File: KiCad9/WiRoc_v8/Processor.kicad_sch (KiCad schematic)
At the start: 21 parts

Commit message: etc
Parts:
- C66, C69, C73, C76, C77, C81, C82, C83: LCSC Part # (none) -> C52923; Manufacturer (none) -> Samsung Electro-Mechanics; ManufacturerPartNumber (none) -> CL05A105KA5NQNC
- C70, C72, C75, C79: LCSC Part # (none) -> C15525; Manufacturer (none) -> Samsung Electro-Mechanics; ManufacturerPartNumber (none) -> CL05A106MQ5NUNC
- U11: value ~ -> AllwinnerH3

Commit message: add bom
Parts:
- C66, C69, C70, C72, C73, C75, C76, C77, C79, C81, C82, C83: IncludeInBOM (none) -> TRUE; JLCBasicExtended (none) -> Basic; Package (none) -> 0402
- C67, C68, C71, C74, C78, C84, C85: IncludeInBOM (none) -> TRUE; JLCBasicExtended (none) -> Basic; LCSC Part # (none) -> C1525; Manufacturer (none) -> Samsung Electro-Mechanics; ManufacturerPartNumber (none) -> CL05B104KO5NNNC; Package (none) -> 0402
- R19: IncludeInBOM (none) -> TRUE; JLCBasicExtended (none) -> Basic; LCSC Part # (none) -> C17168; Manufacturer (none) -> Uniroyal Elec; ManufacturerPartNumber (none) -> 0402WGF0000TCE; Package (none) -> 0402
- U11: IncludeInBOM (none) -> TRUE; JLCBasicExtended (none) -> Extended; LCSC Part # (none) -> C94644; Manufacturer (none) -> Allwinner; ManufacturerPartNumber (none) -> H3; Package (none) -> FBGA-347(14x14)

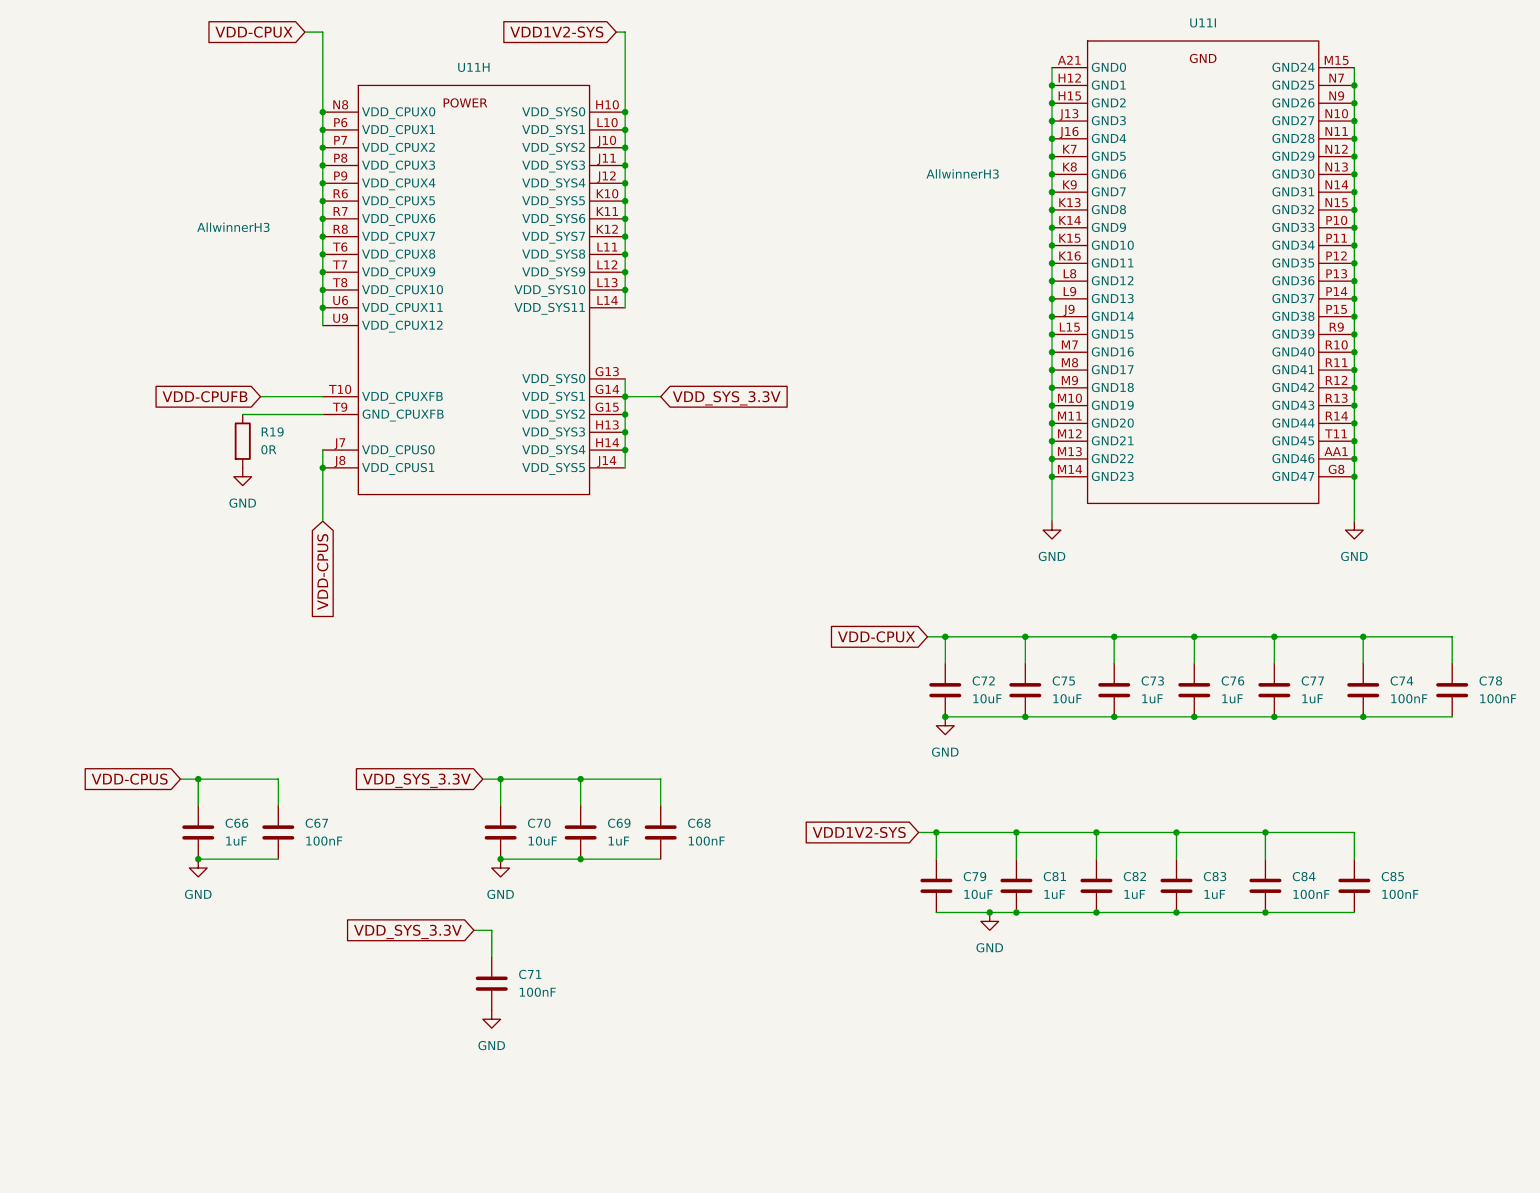
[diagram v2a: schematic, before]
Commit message: add esp32hosted-c5 board
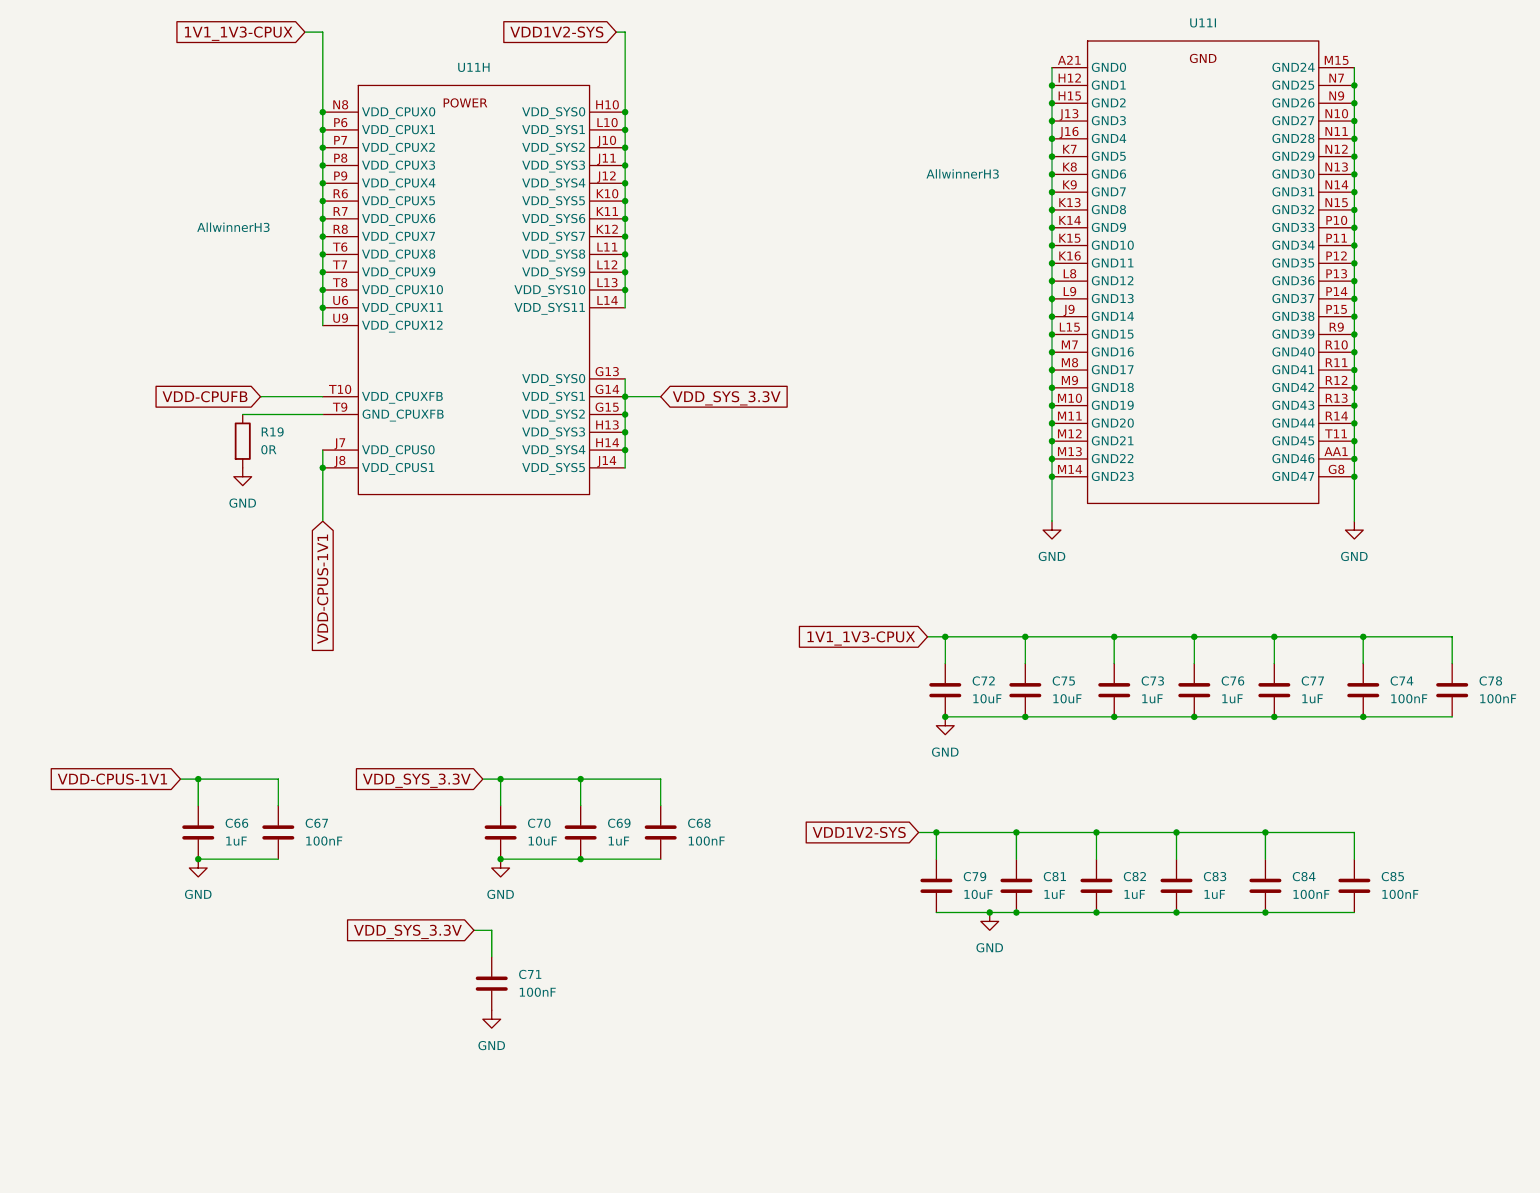
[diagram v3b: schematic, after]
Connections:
- net VDD-CPUS renamed VDD-CPUS-1V1
- net VDD-CPUX renamed 1V1_1V3-CPUX
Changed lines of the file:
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@@
 		)
 	)
-	(global_label "VDD-CPUX"
+	(global_label "1V1_1V3-CPUX"
 		(shape input)
 		(at 138.43 113.03 180)
@@
 		)
 		(property "Intersheetrefs" "${INTERSHEET_REFS}"
-			(at 123.296 113.03 0)
+			(at 118.071 113.03 0)
 			(effects
 				(font
@@
 		)
 	)
-	(global_label "VDD-CPUX"
+	(global_label "1V1_1V3-CPUX"
 		(shape input)
 		(at 49.53 26.67 180)
@@
 		)
 		(property "Intersheetrefs" "${INTERSHEET_REFS}"
-			(at 34.396 26.67 0)
+			(at 29.171 26.67 0)
 			(effects
 				(font
@@
 		)
 	)
-	(global_label "VDD-CPUS"
+	(global_label "VDD-CPUS-1V1"
 		(shape input)
 		(at 31.75 133.35 180)
@@
 		)
 		(property "Intersheetrefs" "${INTERSHEET_REFS}"
-			(at 16.616 133.35 0)
+			(at 10.52 133.35 0)
 			(effects
 				(font
@@
 		)
 	)
-	(global_label "VDD-CPUS"
+	(global_label "VDD-CPUS-1V1"
 		(shape input)
 		(at 52.07 96.52 270)
@@
 		)
 		(property "Intersheetrefs" "${INTERSHEET_REFS}"
-			(at 52.07 111.654 90)
+			(at 52.07 117.75 90)
 			(effects
 				(font

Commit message: change to 10uF in pdn, vdd-dram area to south caps, remove varistor, etc
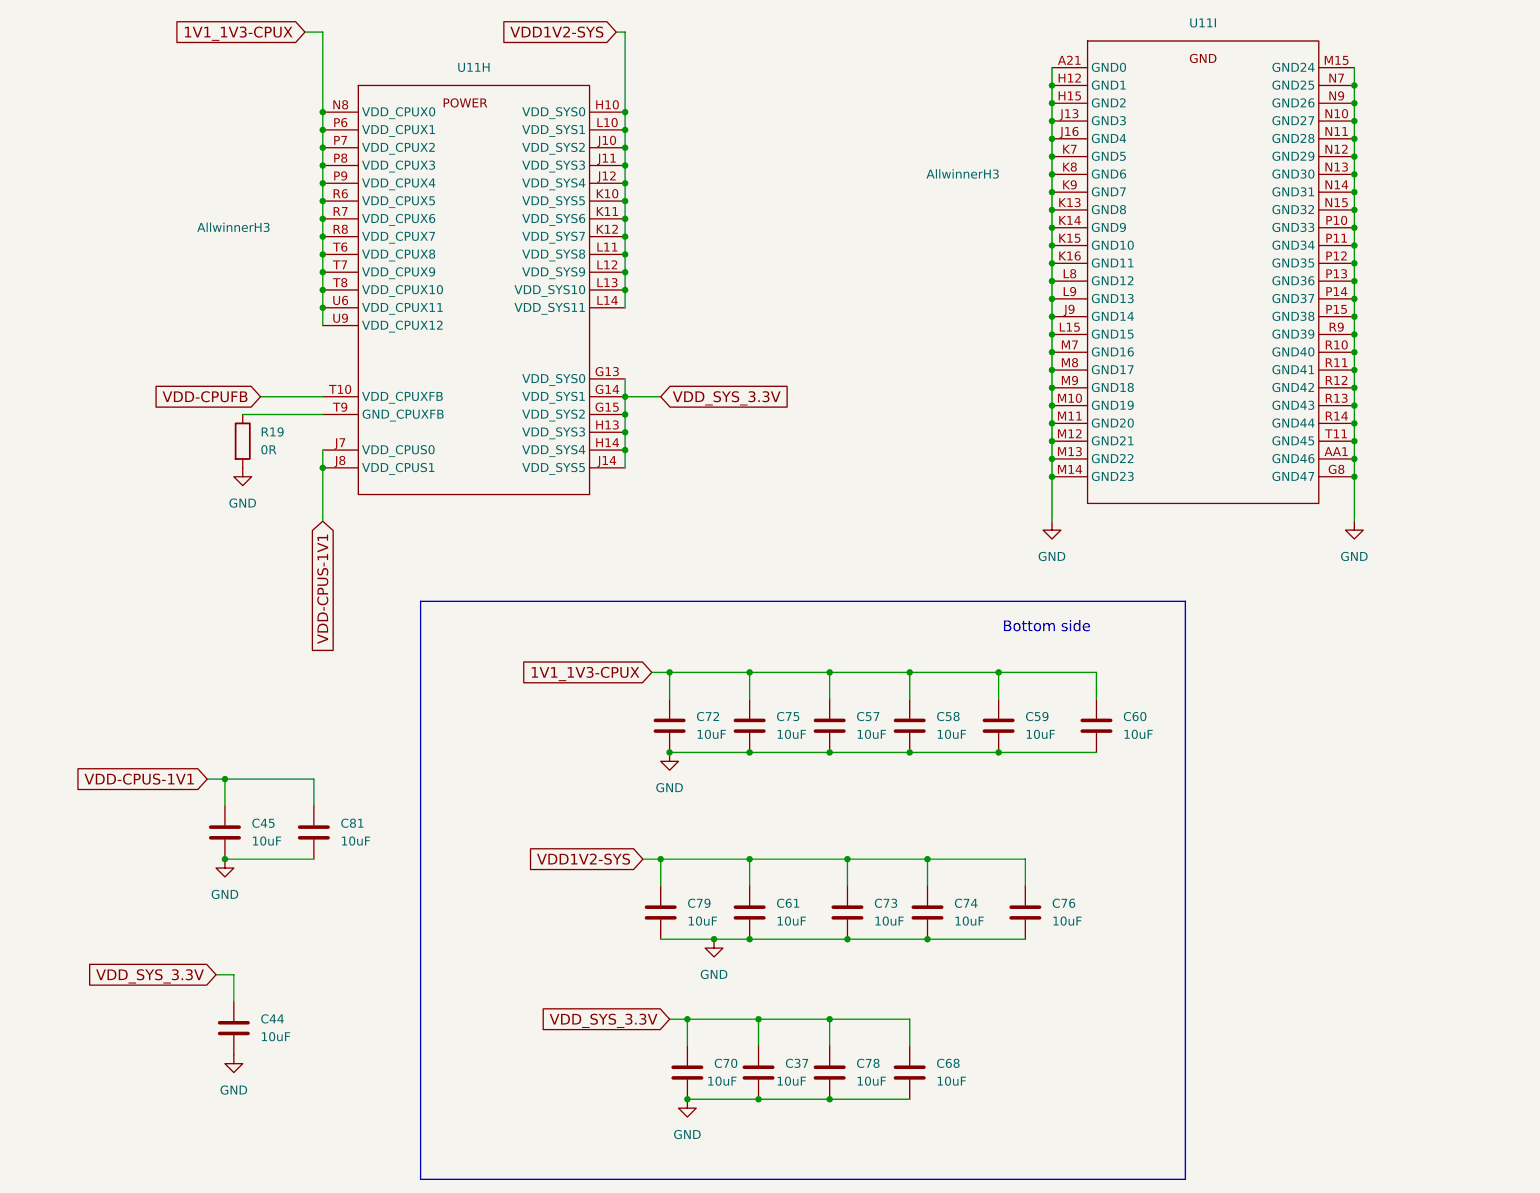
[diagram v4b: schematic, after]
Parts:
- removed C66, C69, C77, C82, C83: 1uF, Capacitor_SMD:C_0402_1005Metric, symbol Device:C
- removed C67, C71, C84, C85: 100nF, Capacitor_SMD:C_0402_1005Metric, symbol Device:C
- added C37, C44, C45, C57, C58, C59, C60, C61: 10uF, Capacitor_SMD:C_0402_1005Metric, symbol Device:C
- C68, C74, C78: value 100nF -> 10uF; LCSC Part # C1525 -> C15525; ManufacturerPartNumber CL05B104KO5NNNC -> CL05A106MQ5NUNC
- C73, C76, C81: value 1uF -> 10uF; LCSC Part # C52923 -> C15525; ManufacturerPartNumber CL05A105KA5NQNC -> CL05A106MQ5NUNC
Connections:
- net 1V1_1V3-CPUX: now also C57.1, C58.1, C59.1, C60.1; no longer C73.1, C74.1, C76.1, C78.1
- net GND: now also C37.2, C44.2, C45.2, C57.2, C58.2, C59.2, C60.2, C61.2
- net VDD-CPUS-1V1: now also C81.1, C45.1
- net VDD1V2-SYS: now also C73.1, C74.1, C76.1, C61.1; no longer C81.1
- net VDD_SYS_3.3V: now also C78.1, C37.1, C44.1
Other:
- note added: "Bottom side"
- moved on the sheet: C70, C72, C75, C79

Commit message: many small changes, change eMMC
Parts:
- C37, C44, C45, C57, C58, C59, C60, C61, C68, C70, C72, C73, C74, C75, C76, C78, C79, C81: value 10uF -> 10uF/6.3V
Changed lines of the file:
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@@
 			)
 		)
-		(property "Value" "10uF"
+		(property "Value" "10uF/6.3V"
 			(at 106.934 176.53 0)
 			(effects
@@
 			)
 		)
-		(property "Value" "10uF"
+		(property "Value" "10uF/6.3V"
 			(at 128.27 127 0)
 			(effects
@@
 			)
 		)
-		(property "Value" "10uF"
+		(property "Value" "10uF/6.3V"
 			(at 54.61 142.24 0)
 			(effects
@@
 			)
 		)
-		(property "Value" "10uF"
+		(property "Value" "10uF/6.3V"
 			(at 43.18 170.18 0)
 			(effects
@@
 			)
 		)
-		(property "Value" "10uF"
+		(property "Value" "10uF/6.3V"
 			(at 166.37 127 0)
 			(effects
@@
 			)
 		)
-		(property "Value" "10uF"
+		(property "Value" "10uF/6.3V"
 			(at 128.27 176.53 0)
 			(effects
@@
 			)
 		)
-		(property "Value" "10uF"
+		(property "Value" "10uF/6.3V"
 			(at 152.4 127 0)
 			(effects
@@
 			)
 		)
-		(property "Value" "10uF"
+		(property "Value" "10uF/6.3V"
 			(at 105.41 127 0)
 			(effects
@@
 			)
 		)
-		(property "Value" "10uF"
+		(property "Value" "10uF/6.3V"
 			(at 41.91 142.24 0)
 			(effects
@@
 			)
 		)
-		(property "Value" "10uF"
+		(property "Value" "10uF/6.3V"
 			(at 130.81 153.67 0)
 			(effects
@@
 			)
 		)
-		(property "Value" "10uF"
+		(property "Value" "10uF/6.3V"
 			(at 116.84 153.67 0)
 			(effects
@@
 			)
 		)
-		(property "Value" "10uF"
+		(property "Value" "10uF/6.3V"
 			(at 139.7 176.53 0)
 			(effects
@@
 			)
 		)
-		(property "Value" "10uF"
+		(property "Value" "10uF/6.3V"
 			(at 142.24 153.67 0)
 			(effects
@@
 			)
 		)
-		(property "Value" "10uF"
+		(property "Value" "10uF/6.3V"
 			(at 139.7 127 0)
 			(effects
@@
 			)
 		)
-		(property "Value" "10uF"
+		(property "Value" "10uF/6.3V"
 			(at 116.84 127 0)
 			(effects
@@
 			)
 		)
-		(property "Value" "10uF"
+		(property "Value" "10uF/6.3V"
 			(at 116.84 176.53 0)
 			(effects
@@
 			)
 		)
-		(property "Value" "10uF"
+		(property "Value" "10uF/6.3V"
 			(at 156.21 153.67 0)
 			(effects
@@
 			)
 		)
-		(property "Value" "10uF"
+		(property "Value" "10uF/6.3V"
 			(at 104.14 153.67 0)
 			(effects

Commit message: etc
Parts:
- removed R19: 0R, Resistor_SMD:R_0402_1005Metric, symbol Device:R
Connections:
- net GND: now also U11.T9 (GND_CPUXFB)
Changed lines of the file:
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@@
-	)
-	(symbol
-		(lib_id "Device:R")
-		(at 40.64 85.09 0)
-		(unit 1)
-		(exclude_from_sim no)
-		(in_bom yes)
-		(on_board yes)
-		(dnp no)
-		(fields_autoplaced yes)
-		(property "Reference" "R19"
-			(at 43.18 83.82 0)
-			(effects
-				(font
-					(size 1.27 1.27)
-				)
-				(justify left)
-			)
-		)
-		(property "Value" "0R"
-			(at 43.18 86.36 0)
-			(effects
-				(font
-					(size 1.27 1.27)
-				)
-				(justify left)
-			)
-		)
-		(property "Footprint" "Resistor_SMD:R_0402_1005Metric"
-			(at 38.862 85.09 90)
-			(effects
-				(font
-					(size 1.27 1.27)
-				)
-				(hide yes)
-			)
-		)
-		(property "Datasheet" "~"
-			(at 40.64 85.09 0)
-			(effects
-				(font
-					(size 1.27 1.27)
-				)
-				(hide yes)
-			)
-		)
-		(property "Description" ""
-			(at 40.64 85.09 0)
-			(effects
-				(font
-					(size 1.27 1.27)
-				)
-				(hide yes)
-			)
-		)
-		(property "JLCBasicExtended" "Basic"
-			(at 40.64 85.09 0)
-			(effects
-				(font
-					(size 1.27 1.27)
-				)
-				(hide yes)
-			)
-		)
-		(property "IncludeInBOM" "TRUE"
-			(at 40.64 85.09 0)
-			(effects
-				(font
-					(size 1.27 1.27)
-				)
-				(hide yes)
-			)
-		)
-		(property "LCSC Part #" "C17168"
-			(at 40.64 85.09 0)
-			(effects
-				(font
-					(size 1.27 1.27)
-				)
-				(hide yes)
-			)
-		)
-		(property "Manufacturer" "Uniroyal Elec"
-			(at 40.64 85.09 0)
-			(effects
-				(font
-					(size 1.27 1.27)
-				)
-				(hide yes)
-			)
-		)
-		(property "ManufacturerPartNumber" "0402WGF0000TCE"
-			(at 40.64 85.09 0)
-			(effects
-				(font
-					(size 1.27 1.27)
-				)
-				(hide yes)
-			)
-		)
-		(property "Package" "0402"
-			(at 40.64 85.09 0)
-			(effects
-				(font
-					(size 1.27 1.27)
-				)
-				(hide yes)
-			)
-		)
-		(pin "1"
-		)
-		(pin "2"
-		)
-		(instances
-			(project "WiRoc_NanoPi"
-				(path "/8ba0b499-eaca-4cd5-a002-c6bdb610cc8c/63531880-33a9-4663-929c-e3626053b78e"
-					(reference "R19")
-					(unit 1)
-				)
-			)
-		)
 	)
 	(symbol
@@
 	(symbol
 		(lib_id "power:GND")
-		(at 40.64 88.9 0)
+		(at 40.64 81.28 0)
 		(unit 1)
 		(exclude_from_sim no)
@@
 		(fields_autoplaced yes)
 		(property "Reference" "#PWR043"
-			(at 40.64 95.25 0)
+			(at 40.64 87.63 0)
 			(effects
 				(font
@@
 		)
 		(property "Value" "GND"
-			(at 40.64 93.98 0)
+			(at 40.64 86.36 0)
 			(effects
 				(font
@@
 		)
 		(property "Footprint" ""
-			(at 40.64 88.9 0)
+			(at 40.64 81.28 0)
 			(effects
 				(font
@@
 		)
 		(property "Datasheet" ""
-			(at 40.64 88.9 0)
+			(at 40.64 81.28 0)
 			(effects
 				(font
@@
 		)
 		(property "Description" ""
-			(at 40.64 88.9 0)
-			(effects
-				(font
+			(at 40.64 81.28 0)
+			(effects
+				(font
